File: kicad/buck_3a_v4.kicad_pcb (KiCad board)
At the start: 2 copper layers, 44 x 44 mm, 25 parts, among them J3 Conn_01x04, J4 Conn_01x02, J5 Conn_01x06, Q1 BSC042NE78NS36, U1 MAX16819ATT+T, U2 ATtiny45-20SU

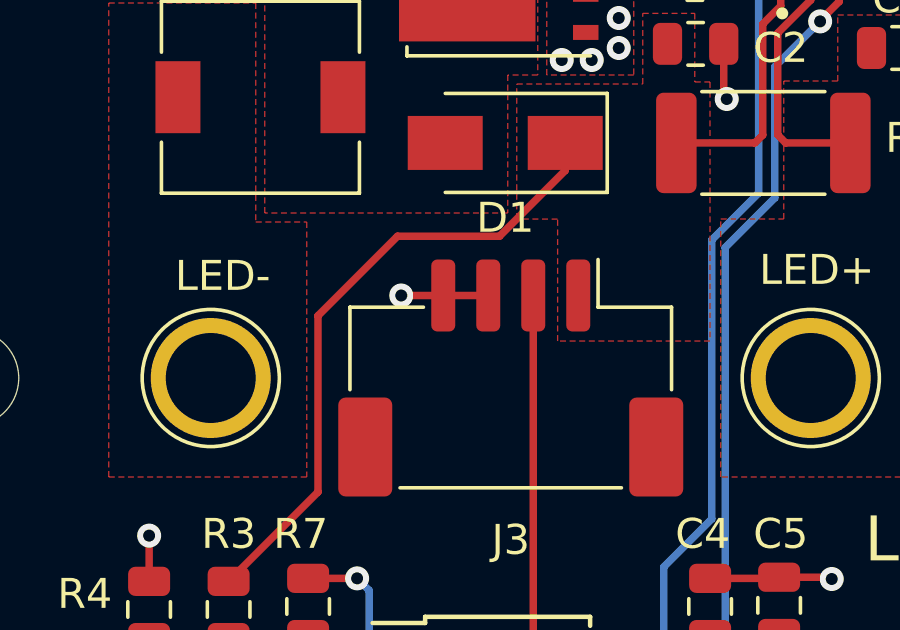
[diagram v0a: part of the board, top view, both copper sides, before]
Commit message: uc_src angepasst
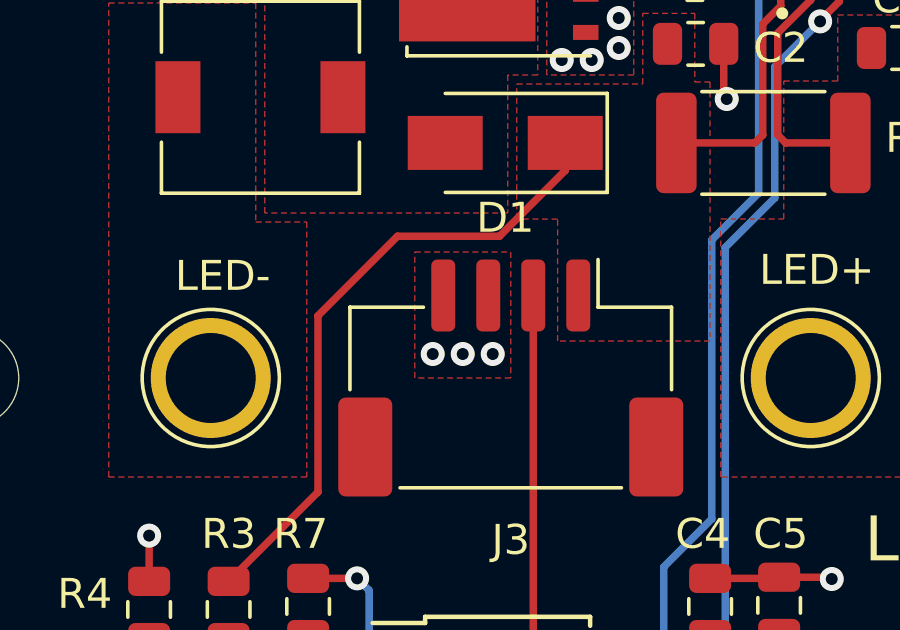
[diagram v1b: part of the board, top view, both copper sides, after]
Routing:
- net GND: track 21.4 -> 18.5 mm, vias 14 -> 16

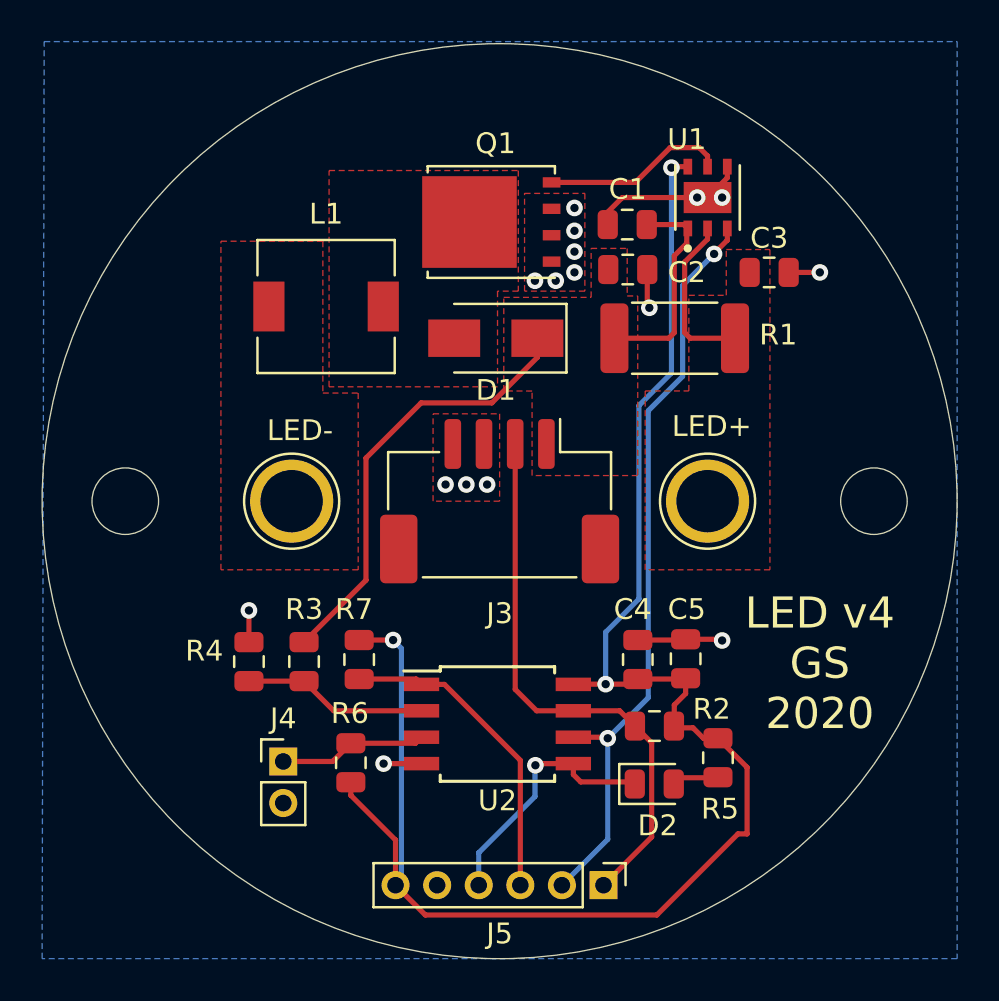
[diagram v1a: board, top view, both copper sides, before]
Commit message: change some parts to non-china parts add some gnd vias to JST connector add new chapter to Aufbau.pdf port uc firmware to new Uc
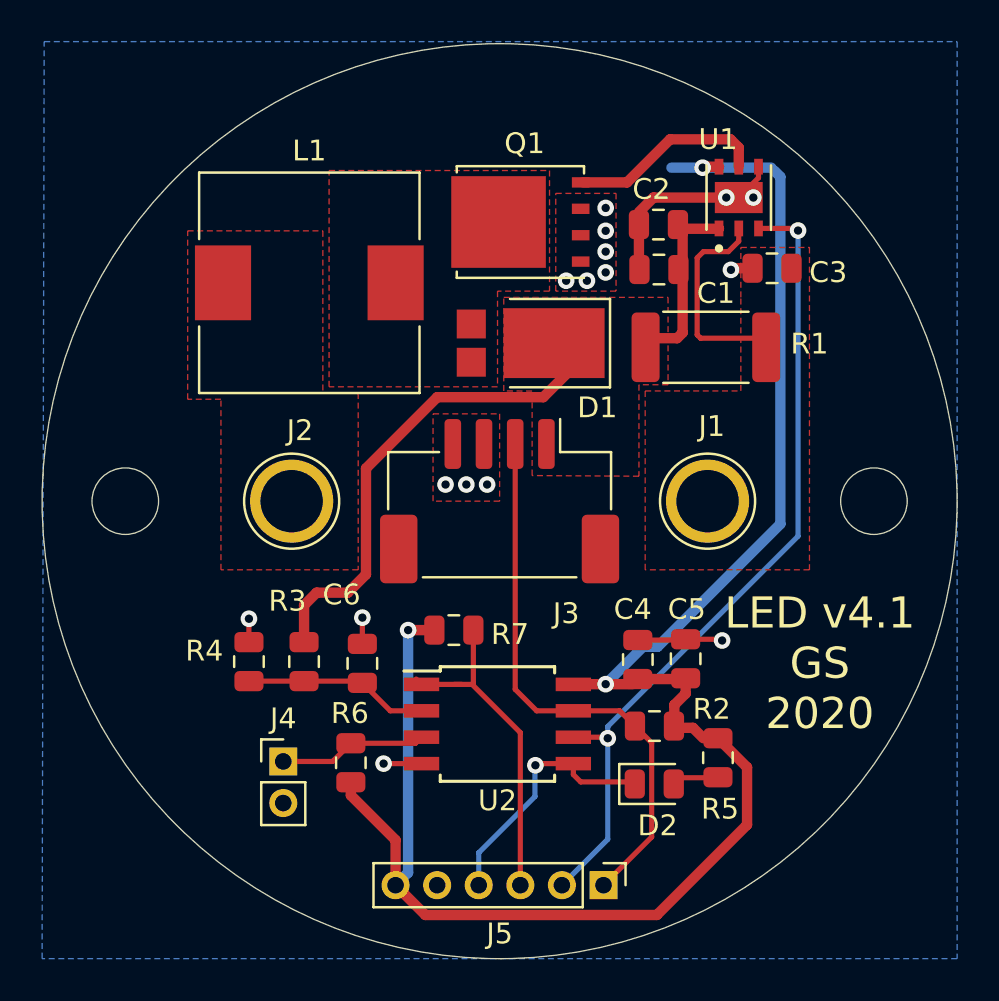
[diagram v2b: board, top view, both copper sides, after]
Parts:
- added C6: 4n70, Capacitor_SMD:C_0805_2012Metric, F.Cu at (43.4, 57.8)
- D1: footprint Diode_SMD:D_SMA -> Diode_SMD:D_PowerDI-5
- L1: footprint Inductor_SMD:L_6.3x6.3_H3 -> Inductor_SMD:L_10.4x10.4_H4.8
- R4: value 8k81 -> 6k81
- moved R7 4.77 mm to (47.8, 56.2), turned to 0 degrees
- moved D1 1.70 mm to (51.5, 42.4)
- moved R1 1.56 mm to (59.9, 42.6)
- moved C1 1.50 mm to (57.7, 38.9), turned to 180 degrees
- moved C2 1.50 mm to (57.6, 36.7)
- moved U1 1.50 mm to (61.5, 35.4)
- moved Q1 1.40 mm to (51.0, 36.6)
- moved L1 1.40 mm to (40.9, 39.5)
- moved C3 0.24 mm to (63.1, 38.8), turned to 180 degrees
- renumbered LED+ to J1, LED- to J2
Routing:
- net +5V: track 81.2 -> 88.6 mm
- net /PWM: track 36.5 -> 39.8 mm
- net Net-(C3-Pad1): track 8.00 -> 10.0 mm
- net VCC: track 31.6 -> 33.2 mm
- net /RESET: track 15.4 -> 16.4 mm
- net GND: track 18.5 -> 19.1 mm
- net Net-(Q1-Pad4): track 8.87 -> 9.44 mm
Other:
- board text added: "LED v4.1 GS 2020"
- board text removed: "LED v4 GS 2020"

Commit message: Fix sleep mode with battery pack
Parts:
- D1: value SS54 -> PDS1040
- L1: value MWSA0603-100MT -> WE7447714100
- Q1: value BSC042NE78NS36 -> BSC050N03
- U1: value MAX16819ATT+T -> MAX16820ATT

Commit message: save
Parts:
- C1: value 22u0 -> 100u/16V; footprint Capacitor_SMD:C_0805_2012Metric -> Capacitor_SMD:C_1210_3225Metric
- C3: value 22u0 -> 100u/16v; footprint Capacitor_SMD:C_0805_2012Metric -> Capacitor_SMD:C_1210_3225Metric
- C4: value 22u0 -> 47u0; footprint Capacitor_SMD:C_0805_2012Metric -> Capacitor_SMD:C_1206_3216Metric
- moved C3 4.76 mm to (62.8, 43.5)
- moved C1 4.71 mm to (58.1, 43.5), turned to 0 degrees
- moved R1 2.79 mm to (60.4, 39.9)
- moved C4 0.22 mm to (56.6, 57.4)
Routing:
- net Net-(C3-Pad1): track 10.0 -> 5.35 mm
- net GND: track 19.1 -> 15.5 mm, vias 16 -> 18
- net +5V: track 88.6 -> 87.1 mm
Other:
- board text added: "LED v4.2 GS 2021"
- board text removed: "LED v4.1 GS 2020"
